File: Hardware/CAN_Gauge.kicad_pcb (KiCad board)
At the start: 2 copper layers, 50 x 50 mm, 72 parts, among them J1 Conn_02x03_Odd_Even, J2 Conn_01x08, SW1 SW_Push, U1 STM32F042K6Ux, U2 SN65HVD230, U3 LMR50410-Q1, U4 UG-2864HSWEG01

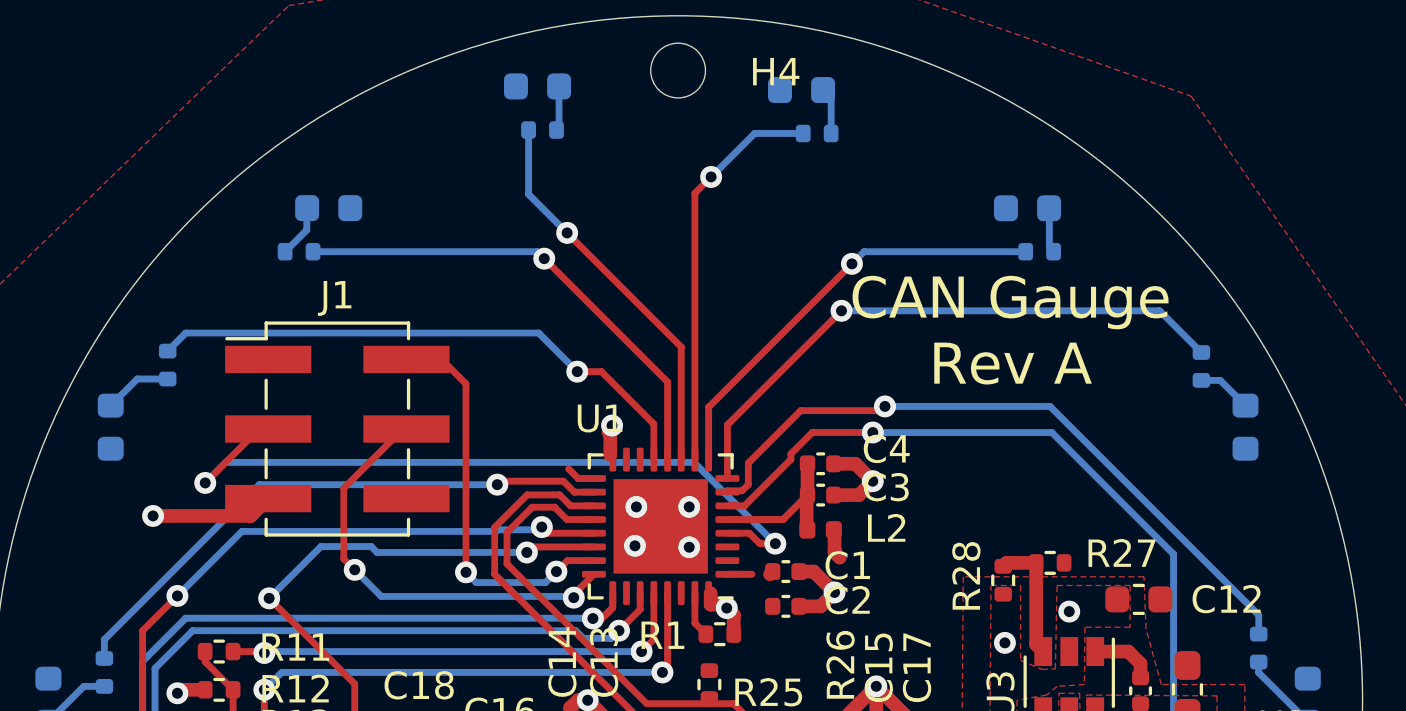
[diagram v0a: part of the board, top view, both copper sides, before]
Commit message: Add config resistors
Add resistors for adjusting configuration settings
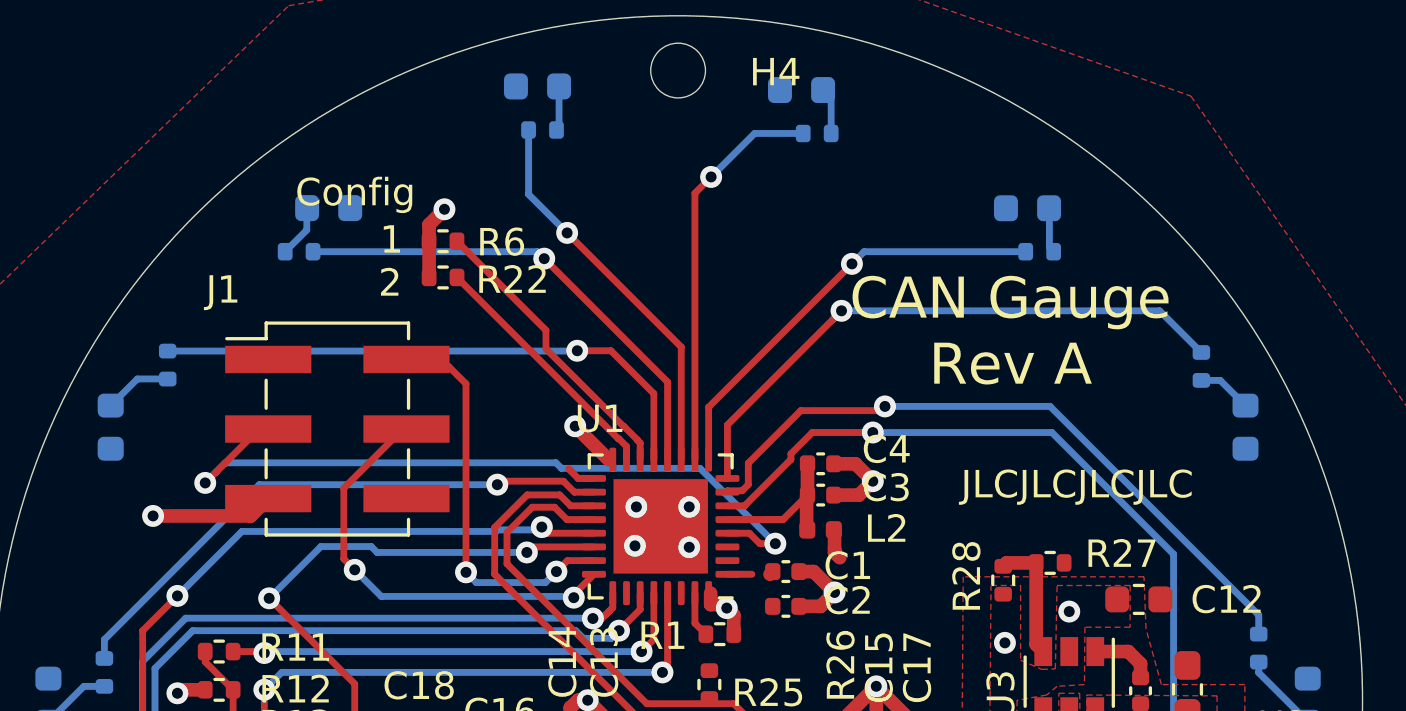
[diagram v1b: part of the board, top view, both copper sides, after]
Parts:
- added R22: 0, Resistor_SMD:R_0402_1005Metric, F.Cu at (124.7, 79.1)
- added R6: 0, Resistor_SMD:R_0402_1005Metric, F.Cu at (124.7, 77.8)
- L2: value 10uH -> 30
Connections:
- U1 pad 14: Net-(U1-Pad14) -> /STM/CONFIG_1
- U1 pad 15: Net-(U1-Pad15) -> /STM/CONFIG_2
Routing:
- net /STM/CONFIG_1: track 0.00 -> 10.8 mm
- net /STM/CONFIG_2: track 0.00 -> 9.23 mm
- net GND: track 67.6 -> 70.9 mm, vias 26 -> 27
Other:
- board text added: "1"
- board text added: "2"
- board text added: "Config"
- board text added: "JLCJLCJLCJLC"

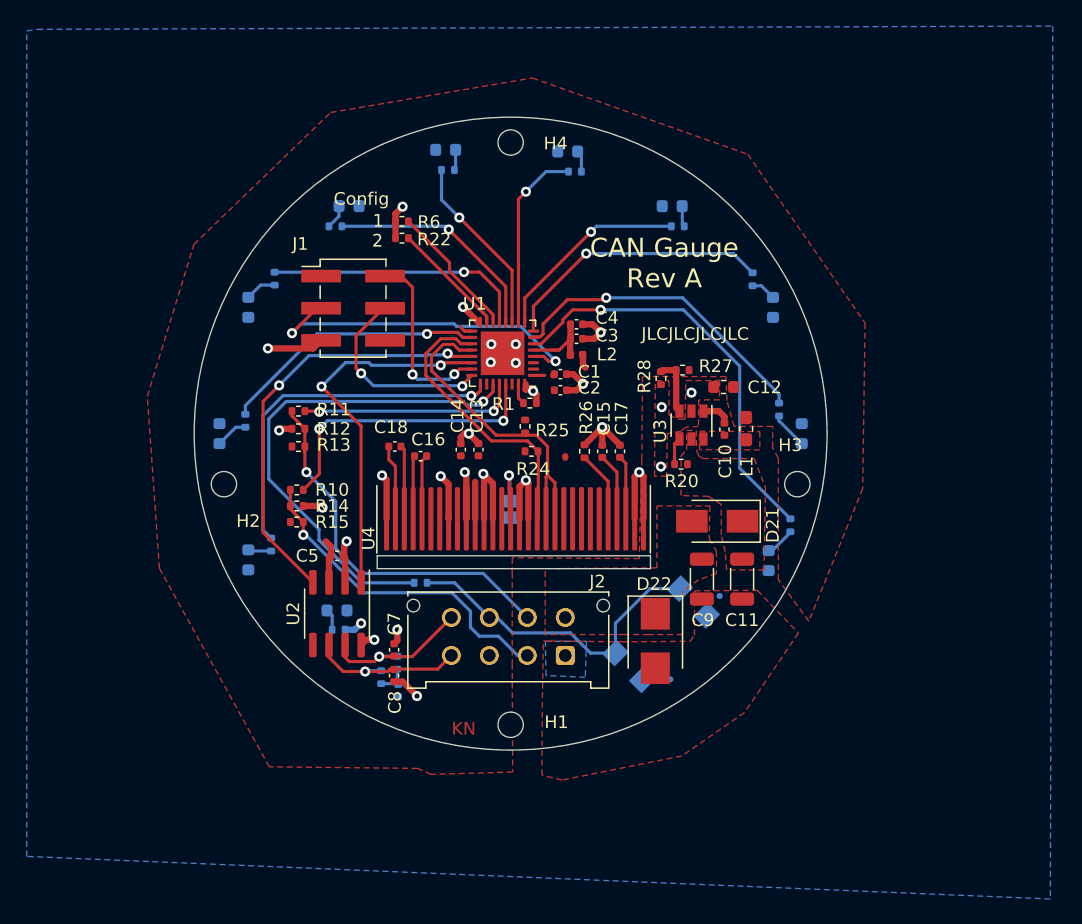
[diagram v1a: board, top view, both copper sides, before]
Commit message: Rev B
Update STM package, switcher circuit, layout
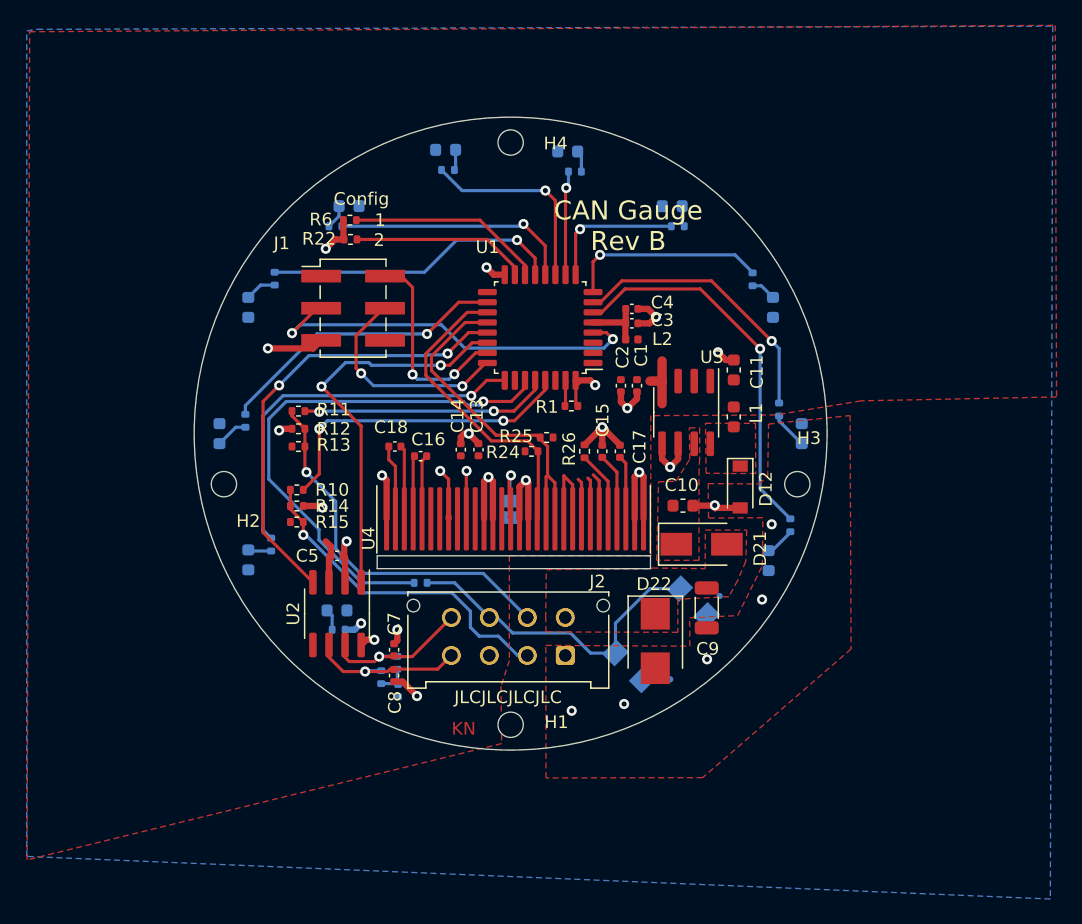
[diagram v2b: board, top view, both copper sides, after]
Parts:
- removed C12: 10u, Inductor_SMD:L_0603_1608Metric
- removed R20, R28: 22.1k, Resistor_SMD:R_0402_1005Metric
- removed R27: 51k, Resistor_SMD:R_0402_1005Metric
- added D12: 1N5817, Diode_SMD:D_SOD-123, F.Cu at (151.4, 98.8)
- C10: value 0.1u -> 63u; footprint Capacitor_SMD:C_0402_1005Metric -> Inductor_SMD:L_0603_1608Metric
- C11: value 2.2u -> 120u; footprint Inductor_SMD:L_1206_3216Metric -> Inductor_SMD:L_0603_1608Metric
- L1: value 3.3u -> 100mH; footprint Inductor_SMD:L_0603_1608Metric_Pad1.05x0.95mm_HandSolder -> Inductor_SMD:L_0603_1608Metric
- R22, R6: value 0 -> 10
- U1: value STM32F042K6Ux -> STM32F042K6Tx; footprint Package_DFN_QFN:QFN-32-1EP_5x5mm_P0.5mm_EP3.45x3.45mm -> Package_QFP:LQFP-32_7x7mm_P0.8mm
- U3: value LMR50410-Q1 -> 2594; footprint Package_TO_SOT_SMD:SOT-23-6 -> Package_SO:SOIC-8_3.9x4.9mm_P1.27mm
- moved C11 16.5 mm to (150.9, 89.6), turned to 90 degrees
- moved C10 6.87 mm to (146.9, 100.3), turned to 0 degrees
- moved C1 6.11 mm to (143.3, 90.8), turned to 270 degrees
- moved C2 4.79 mm to (142.0, 90.8), turned to 270 degrees
- moved L2 4.54 mm to (142.9, 87.1)
- moved C3 4.54 mm to (142.9, 85.9)
- moved C4 4.54 mm to (142.9, 84.7)
- moved R6 4.11 mm to (120.6, 77.7)
- moved R22 4.07 mm to (120.7, 79.3)
- moved U1 3.60 mm to (135.6, 86.2)
- moved R1 3.28 mm to (138.1, 92.4)
- moved C9 2.31 mm to (148.8, 108.4)
- moved D21 2.19 mm to (148.4, 103.3), turned to 0 degrees
- moved R25 1.91 mm to (136.1, 94.9), turned to 0 degrees
- moved L1 1.35 mm to (150.9, 93.3)
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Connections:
- C10 pad 1: Net-(C10-Pad1) -> +12V
- C10 pad 2: Net-(C10-Pad2) -> GND
- C11 pad 1: +12V -> +3V3
- L1 pad 1: Net-(C10-Pad2) -> Net-(D12-Pad1)
- U3 pad 1: Net-(C10-Pad1) -> (no net)
- U3 pad 2: GND -> (no net)
- U3 pad 3: Net-(R27-Pad2) -> (no net)
- U3 pad 4: Net-(R20-Pad2) -> +3V3
- U3 pad 5: +12V -> GND
- U3 pad 6: Net-(C10-Pad2) -> GND
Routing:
- net +3V3: track 11.2 -> 26.8 mm
- net GND: track 70.9 -> 80.2 mm, vias 27 -> 28
- net LED5: track 14.6 -> 8.24 mm
- net LED3: track 22.1 -> 15.8 mm
- net NRST: track 27.4 -> 32.6 mm
- net LED4: track 16.2 -> 11.0 mm
- net /STM/CONFIG_1: track 10.8 -> 15.6 mm
- net /STM/CONFIG_2: track 9.23 -> 14.0 mm
- net Net-(R27-Pad2): track 4.60 -> 0.00 mm
- net LED2: track 25.1 -> 21.9 mm
- net LED1: track 33.1 -> 30.3 mm
- net LED8: track 20.8 -> 23.5 mm
- net SPARE_1_IN: track 17.3 -> 19.9 mm
- net USER_INPUT: track 39.8 -> 42.2 mm
- net SPARE_2_IN: track 23.1 -> 25.5 mm
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- added copper zone on F.Cu, net Net-(D12-Pad1)
- removed copper zone on F.Cu, net Net-(C10-Pad2)
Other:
- board text added: "CAN Gauge Rev B"
- board text removed: "CAN Gauge Rev A"

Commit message: Update components for assembly, generate gerbers
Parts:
- C10: value 63u -> 10u
- C11: footprint Inductor_SMD:L_0603_1608Metric -> Capacitor_SMD:C_1206_3216Metric
- L1: value 100mH -> 100uH; footprint Inductor_SMD:L_0603_1608Metric -> Inductor_SMD:L_0805_2012Metric
- R22, R6: value 10 -> 10k
- R9: value 10k -> 1k
- SW1: footprint Button_Switch_SMD:SW_SPST_TL3305A -> Button_Switch_SMD:SW_Push_1P1T_NO_6x6mm_H9.5mm
- moved C1 16.5 mm to (130.1, 80.9), turned to 90 degrees
- moved C11 2.38 mm to (149.8, 87.5), turned to 180 degrees
- moved L1 0.70 mm to (151.6, 93.4)
- moved C2 0.13 mm to (142.0, 90.7)
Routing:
- net LED1: track 30.3 -> 33.4 mm
- net +3V3: track 26.8 -> 29.3 mm
- net LED2: track 21.9 -> 23.6 mm
- net GND: track 80.2 -> 81.5 mm
- net BTN_IN: track 25.8 -> 24.8 mm
- net /STM/CONFIG_2: track 14.0 -> 14.8 mm
- net NRST: track 32.6 -> 32.0 mm
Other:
- net class I2C added: clearance 0.2, trace_width 0.25, via_dia 0.8, via_drill 0.4
- board text added: "github.com Keith-N/STM-CAN-Gauge"

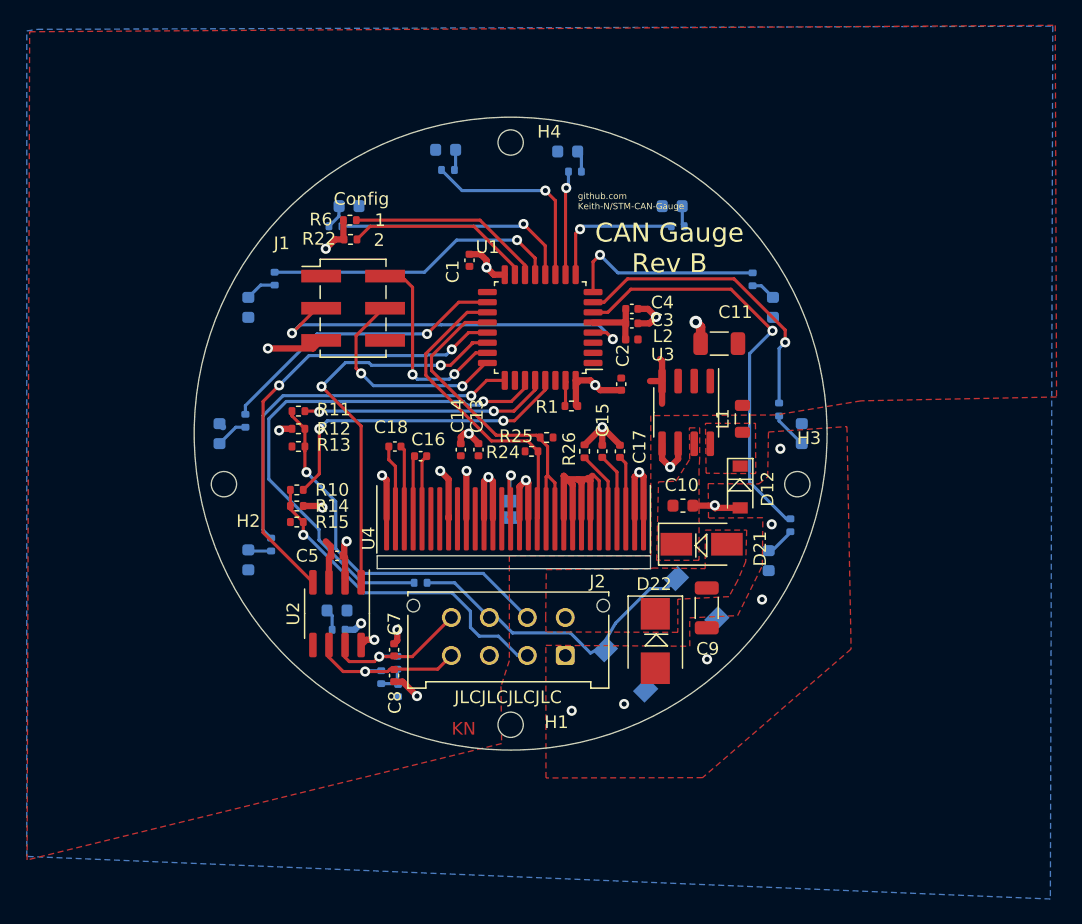
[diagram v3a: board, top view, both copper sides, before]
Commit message: Update board layout
Fix OLED pads to meet intended design. Move all non UI components to one side of the board for better single sided assembly.
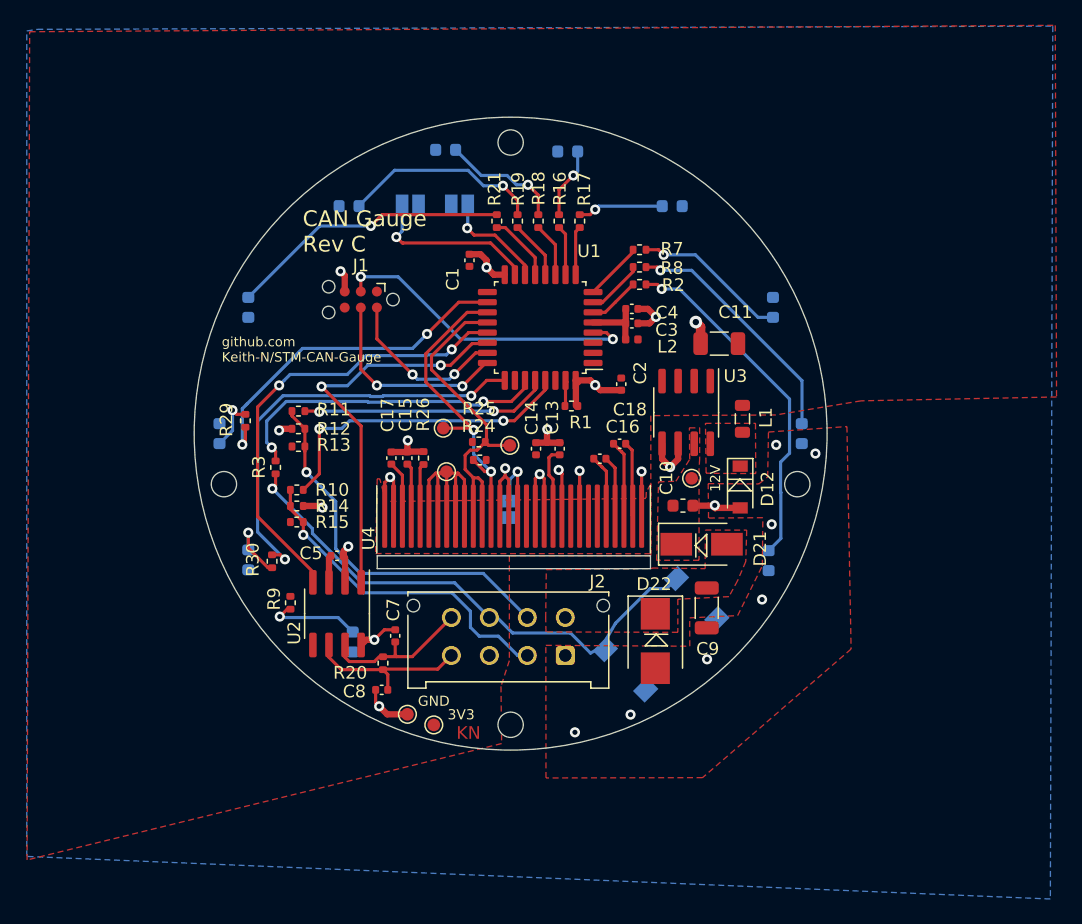
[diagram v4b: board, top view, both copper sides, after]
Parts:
- removed C6: 0.1u, Capacitor_SMD:C_0402_1005Metric
- removed R22, R6: 10k, Resistor_SMD:R_0402_1005Metric
- removed R4, R5: 60, Resistor_SMD:R_0402_1005Metric
- added JP2: SolderJumper_2_Open, Jumper:SolderJumper-2_P1.3mm_Open_Pad1.0x1.5mm, B.Cu at (129.3, 76.5)
- added JP3: SolderJumper_2_Open, Jumper:SolderJumper-2_P1.3mm_Open_Pad1.0x1.5mm, B.Cu at (125.4, 76.5)
- added R20: 120, Resistor_SMD:R_0402_1005Metric, F.Cu at (123.2, 112.7)
- added TP1: TestPoint, TestPoint:TestPoint_Pad_D1.0mm, F.Cu at (128.0, 94.2)
- added TP2: TestPoint, TestPoint:TestPoint_Pad_D1.0mm, F.Cu at (133.2, 95.5)
- added TP3: TestPoint, TestPoint:TestPoint_Pad_D1.0mm, F.Cu at (147.6, 98.1)
- added TP4: TestPoint, TestPoint:TestPoint_Pad_D1.0mm, F.Cu at (127.2, 117.6)
- added TP5: TestPoint, TestPoint:TestPoint_Pad_D1.0mm, F.Cu at (125.2, 116.8)
- added TP6: TestPoint, TestPoint:TestPoint_Pad_D1.0mm, F.Cu at (128.2, 97.6)
- J1: footprint Connector_PinHeader_2.54mm:PinHeader_2x03_P2.54mm_Vertical_SMD -> Connector:Tag-Connect_TC2030-IDC-NL_2x03_P1.27mm_Vertical
- R16, R17, R18, R19, R2, R21, R29, R3, R30, R7, R8, R9: moved to F.Cu
- moved R2 22.4 mm to (143.5, 82.8), turned to 180 degrees
- moved R21 18.1 mm to (132.2, 77.8), turned to 270 degrees
- moved C17 18.1 mm to (123.9, 96.5)
- moved C18 17.8 mm to (141.9, 95.4), turned to 0 degrees
- moved R8 15.8 mm to (143.5, 81.4), turned to 180 degrees
- moved C15 15.4 mm to (125.1, 96.5)
- moved R3 14.6 mm to (114.7, 97.3), turned to 90 degrees
- moved R19 14.4 mm to (133.9, 77.8), turned to 270 degrees
- moved C16 14.2 mm to (140.4, 96.6), turned to 0 degrees
- moved R26 12.7 mm to (126.4, 96.5)
- moved R7 9.23 mm to (143.5, 80.1), turned to 180 degrees
- moved R18 8.20 mm to (135.5, 77.8), turned to 270 degrees
- moved R17 7.76 mm to (138.8, 77.8), turned to 270 degrees
- moved C13 6.41 mm to (137.2, 95.8)
- moved C14 5.94 mm to (135.3, 95.8)
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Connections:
- U4 pad 21: +3V3 -> Net-(TP6-Pad1)
- U4 pad 22: +3V3 -> Net-(TP6-Pad1)
- U4 pad 23: +3V3 -> Net-(TP6-Pad1)
- U4 pad 24: +3V3 -> Net-(TP6-Pad1)
- U4 pad 25: +3V3 -> Net-(TP6-Pad1)
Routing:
- net LED1: track 33.4 -> 4.08 mm, vias 1 -> 0
- net Net-(D1-Pad2): track 2.01 -> 27.8 mm, vias 0 -> 1
- net Net-(D8-Pad2): track 2.48 -> 22.3 mm, vias 0 -> 1
- net Net-(TP6-Pad1): track 0.00 -> 19.8 mm
- net LED2: track 23.6 -> 4.52 mm, vias 1 -> 0
- net LED8: track 23.5 -> 5.37 mm, vias 1 -> 0
- net BTN_IN: track 24.8 -> 41.6 mm, vias 0 -> 1
- net Net-(D2-Pad2): track 2.92 -> 19.5 mm, vias 0 -> 1
- net USER_INPUT: track 42.2 -> 25.8 mm, vias 1 -> 2
- net +3V3: track 29.3 -> 14.4 mm, vias 1 -> 0
- net LED7: track 19.1 -> 4.63 mm, vias 1 -> 0
- net Net-(D7-Pad2): track 1.92 -> 15.8 mm, vias 0 -> 1
- net LED6: track 15.9 -> 4.28 mm, vias 1 -> 0
- net LED3: track 15.8 -> 4.66 mm, vias 1 -> 0
- net Net-(D3-Pad2): track 1.99 -> 12.2 mm, vias 0 -> 1
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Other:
- board text added: "12V"
- board text added: "3V3"
- board text added: "Add Sel"
- board text added: "CAN Gauge Rev C"
- board text added: "GND"
- board text removed: "CAN Gauge Rev B"

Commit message: Updates
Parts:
- added TP7: TestPoint, TestPoint:TestPoint_Pad_D1.0mm, F.Cu at (139.0, 95.2)
- added TP8: TestPoint, TestPoint:TestPoint_Pad_D1.0mm, F.Cu at (128.1, 95.5)
- C10: footprint Inductor_SMD:L_0603_1608Metric -> Inductor_SMD:L_1206_3216Metric
- C13: value 1u -> 0.1u
- C7, C8: value 0.1u -> 0
- R16: value 100 -> 1k
- moved TP1 1.34 mm to (126.9, 93.4)
- moved C10 1.01 mm to (147.9, 100.0)
- moved TP3 0.41 mm to (147.5, 97.7)
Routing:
- net I2C1_SCL: track 27.8 -> 29.2 mm

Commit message: Update for F103
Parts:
- U1: value STM32F042K6Tx -> STM32F103C8Tx; footprint Package_QFP:LQFP-32_7x7mm_P0.8mm -> Package_QFP:LQFP-48_7x7mm_P0.5mm
- moved C2 1.59 mm to (140.5, 90.5)
- moved U1 1.55 mm to (136.3, 84.8)
- moved R18 1.09 mm to (135.3, 76.7)
- moved R21 1.09 mm to (132.0, 76.7)
- moved R16 1.09 mm to (136.9, 76.7)
- moved R17 1.09 mm to (138.6, 76.7)
- moved R19 1.09 mm to (133.7, 76.7)
- moved C1 1.02 mm to (130.4, 79.9), turned to 180 degrees
- moved C3 0.53 mm to (143.4, 86.0)
- moved C4 0.53 mm to (143.4, 84.9)
- moved L2 0.53 mm to (143.4, 87.3)
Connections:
- net Net-(U1-Pad3) renamed OSC_IN
- U1 pad 1: +3V3 -> Net-(U1-Pad1)
- U1 pad 10: LED5 -> LED1
- U1 pad 11: LED6 -> LED2
- U1 pad 12: LED7 -> LED3
- U1 pad 13: LED8 -> LED4
- U1 pad 14: /STM/CONFIG_1 -> LED5
- U1 pad 15: /STM/CONFIG_2 -> LED6
- U1 pad 16: GND -> LED7
- U1 pad 17: +3V3 -> LED8
- U1 pad 18: LED9 -> /STM/CONFIG_1
- U1 pad 19: I2C1_SCL -> /STM/CONFIG_2
- U1 pad 20: I2C1_SDA -> Net-(U1-Pad20)
- U1 pad 21: CAN_RX -> Net-(U1-Pad21)
- U1 pad 22: CAN_TX -> Net-(U1-Pad22)
- U1 pad 23: SWDIO -> GND
- U1 pad 24: SWCLK -> +3V3
- U1 pad 25: LED10 -> Net-(U1-Pad25)
- U1 pad 27: USER_INPUT -> Net-(U1-Pad27)
- U1 pad 28: SPARE_1_IN -> Net-(U1-Pad28)
- U1 pad 29: SPARE_2_IN -> LED9
- U1 pad 30: Net-(U1-Pad30) -> LED10
- U1 pad 31: BOOT0 -> Net-(U1-Pad31)
- U1 pad 32: GND -> CAN_RX
- U1 pad 4: NRST -> OSC_OUT
- U1 pad 5: VDDA -> Net-(U1-Pad5)
- U1 pad 6: LED1 -> Net-(U1-Pad6)
- U1 pad 7: LED2 -> NRST
- U1 pad 8: LED3 -> GND
- U1 pad 9: LED4 -> VDDA
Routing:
- net GND: track 75.6 -> 84.2 mm, vias 27 -> 29
- net LED10: track 33.9 -> 40.6 mm
- net +3V3: track 14.4 -> 19.2 mm
- net I2C1_SDA: track 26.8 -> 22.5 mm
- net I2C1_SCL: track 29.2 -> 25.0 mm
- net /STM/CONFIG_1: track 8.45 -> 11.3 mm
- net Net-(D8-Pad2): track 22.3 -> 24.7 mm
- net SWCLK: track 16.3 -> 18.3 mm
- net SWDIO: track 13.4 -> 15.3 mm
- net LED8: track 5.37 -> 7.20 mm
- net BOOT0: track 2.23 -> 3.77 mm
- net VDDA: track 5.04 -> 6.57 mm
- net LED7: track 4.63 -> 6.14 mm
- net LED2: track 4.52 -> 3.02 mm
- net LED1: track 4.08 -> 2.66 mm
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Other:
- board text added: "CAN Gauge 103_A"
- board text removed: "CAN Gauge Rev C"
